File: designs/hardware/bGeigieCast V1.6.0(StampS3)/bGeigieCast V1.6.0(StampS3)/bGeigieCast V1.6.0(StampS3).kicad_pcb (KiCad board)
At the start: 2 copper layers, 25 x 27.4 mm, 3 parts, among them J1 Left, J2 Right, U2 XBEE-socket

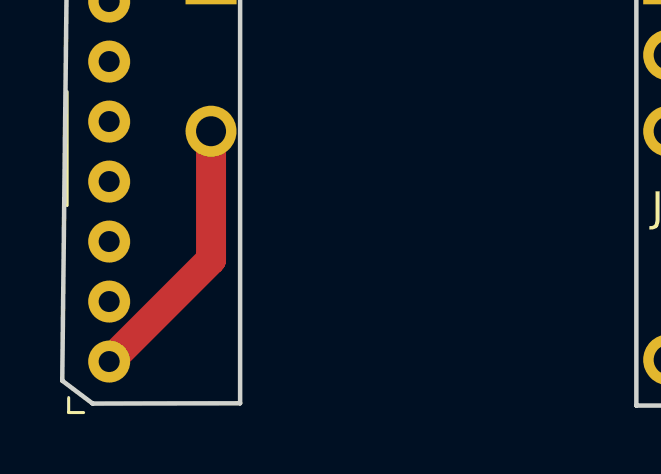
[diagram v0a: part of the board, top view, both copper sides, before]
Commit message: Added new board V1.6.1 for M5stampS3 and M5stamp pico
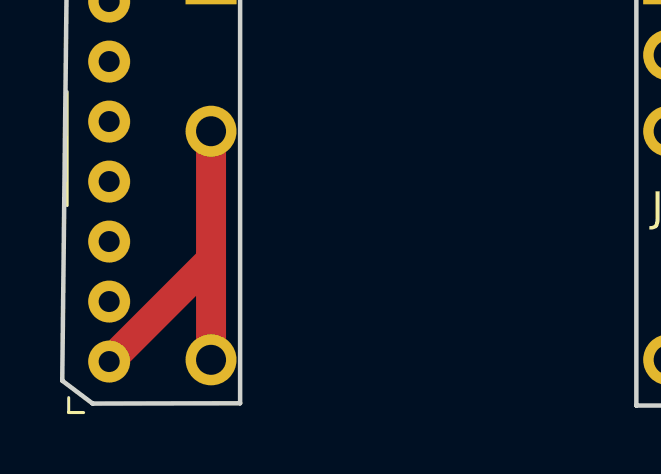
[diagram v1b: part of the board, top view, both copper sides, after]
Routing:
- net GND: track 9.08 -> 12.4 mm
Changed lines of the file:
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@@
       (plotreference true)
       (plotvalue true)
+      (plotfptext true)
       (plotinvisibletext false)
       (sketchpadsonfab false)
@@
       (net 18 "GND")
     )
+    (pad "6" thru_hole oval (at 0 12.7) (size 1.7 1.7) (drill 1) (layers "*.Cu" "*.Mask")
+      (net 18 "GND")
+    )
     (model "${KICAD7_3DMODEL_DIR}/Connector_PinHeader_2.54mm.3dshapes/PinHeader_1x01_P2.54mm_Vertical.wrl"
       (offset (xyz 0 0 -3))
@@
   (segment (start 140.796 113.954) (end 140.796 109.672) (width 1) (layer "F.Cu") (net 18))
   (segment (start 137.4 117.35) (end 140.796 113.954) (width 1) (layer "F.Cu") (net 18))
+  (segment (start 140.796 113.954) (end 140.796 117.292) (width 1) (layer "F.Cu") (net 18))
   (segment (start 153.984557 93.316557) (end 143.515443 93.316557) (width 1) (layer "F.Cu") (net 19))
   (segment (start 143.515443 93.316557) (end 143.416 93.416) (width 1) (layer "F.Cu") (net 19))
